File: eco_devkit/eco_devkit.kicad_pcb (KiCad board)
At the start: 2 copper layers, 98.5 x 78 mm, 144 parts, among them J1 USB_C_Receptacle_USB2.0_16P, J10 Micro_SD_Card_Det1, J11 DISPLAY FFC, J2 Conn_02x20_Counter_Clockwise, J3 ADC_SEL1, J4 BluetoothHeader, J5 ADC_SEL1, J6 ADC_SEL1, J7 ADC_SEL1, J8 USB_C_Receptacle_USB2.0_16P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

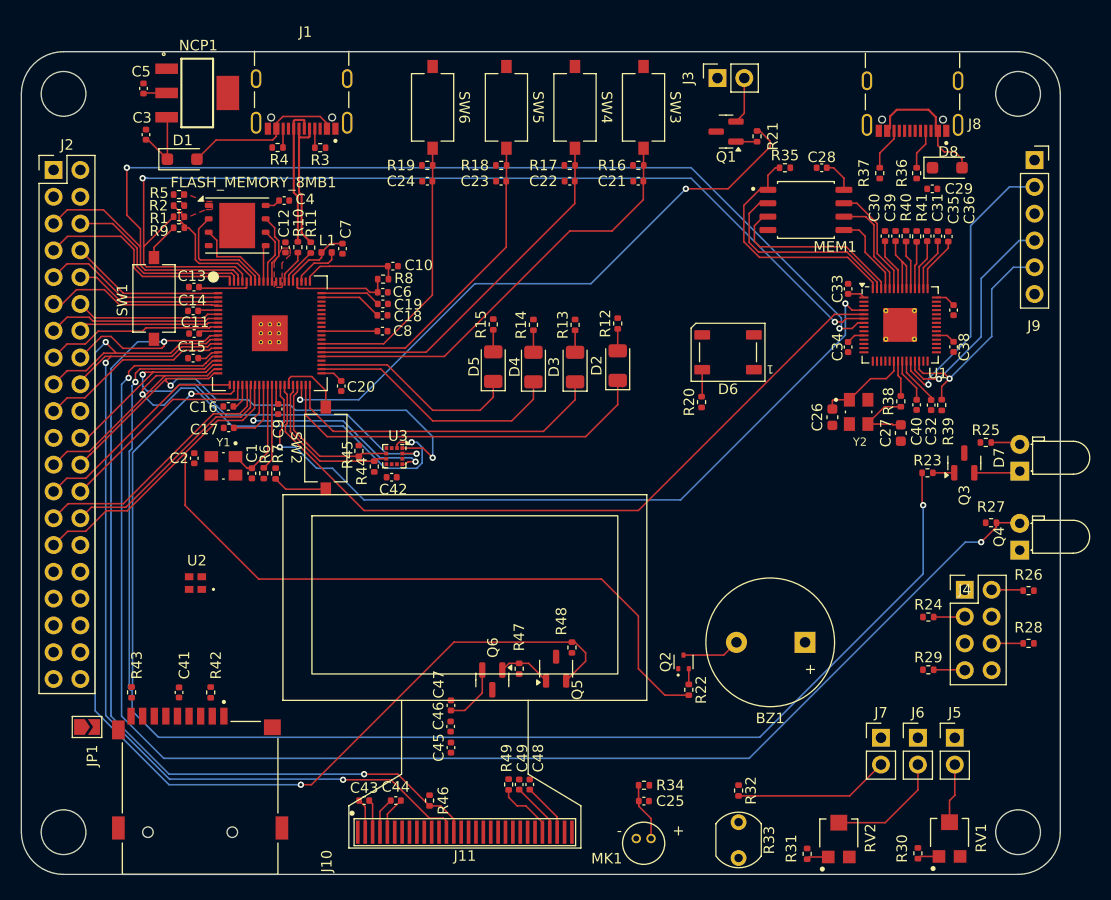
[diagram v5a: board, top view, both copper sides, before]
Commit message: Add all nets
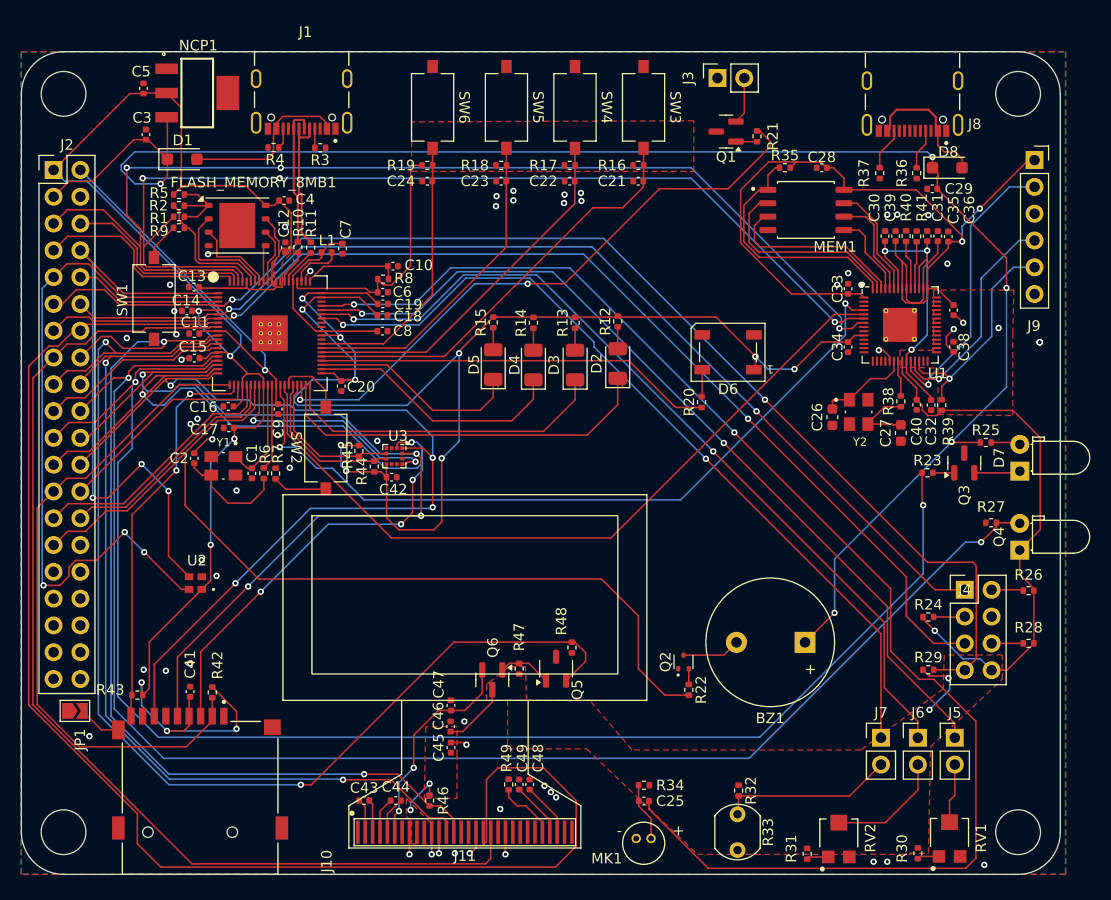
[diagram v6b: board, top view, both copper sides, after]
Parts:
- moved JP1 1.91 mm to (105.1, 112.5)
- moved C41 1.05 mm to (116.0, 110.7), turned to -90 degrees
- moved R33 0.76 mm to (167.9, 122.3)
- moved R43 0.61 mm to (111.0, 111.0), turned to 180 degrees
- moved C14 0.58 mm to (115.7, 74.6)
- moved R4 0.39 mm to (123.9, 59.1)
- moved D3 0.19 mm to (152.5, 79.7)
- moved D4 0.19 mm to (148.6, 79.7)
- moved R13 0.19 mm to (152.5, 75.7)
- moved R14 0.19 mm to (148.6, 75.7)
- moved D2 0.19 mm to (156.5, 79.6)
- moved D5 0.19 mm to (144.7, 79.7)
- moved R12 0.19 mm to (156.5, 75.6)
- moved R15 0.19 mm to (144.7, 75.7)
- moved R42 0.15 mm to (118.1, 110.8)
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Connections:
- C25 pad 2: GPIO44_ADC4 -> GPIO46_ADC6
- C30 pad 1: +1V1 -> +1V1_PROBE
- C31 pad 1: +1V1 -> +1V1_PROBE
- C32 pad 2: +1V1 -> +1V1_PROBE
- J2 pad 40: GPIO43_ADC3 -> GPIO45_ADC5
- J5 pad 1: GPIO43_ADC3 -> GPIO45_ADC5
- J6 pad 1: GPIO45_ADC5 -> GPIO44_ADC4
- J7 pad 1: GPIO46_ADC6 -> GPIO43_ADC3
- RP2350B1 pad 58: GPIO43_ADC3 -> GPIO45_ADC5
- U1 pad 23: +1V1 -> +1V1_PROBE
- U1 pad 45: +1V1 -> +1V1_PROBE
- U1 pad 50: +1V1 -> +1V1_PROBE
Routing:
- net +3V3: track 78.0 -> 481.9 mm, vias 0 -> 24
- net +VBUS: track 6.81 -> 162.4 mm, vias 0 -> 5
- net GPIO46_ADC6: track 0.00 -> 132.2 mm, vias 0 -> 2
- net DISPLAY_SCK: track 14.3 -> 135.6 mm
- net PIN_WIFI_RESET_BL: track 19.8 -> 117.5 mm, vias 0 -> 2
- net PIN_WIFI_TX: track 16.4 -> 107.2 mm, vias 0 -> 2
- net PIN_WIFI_RX: track 13.8 -> 100.7 mm, vias 0 -> 2
- net DISPLAY_MOSI: track 16.9 -> 103.0 mm
- net GPIO45_ADC5: track 0.00 -> 83.7 mm, vias 0 -> 2
- net GPIO44_ADC4: track 0.00 -> 81.2 mm, vias 0 -> 2
- net GPIO43_ADC3: track 0.00 -> 79.3 mm, vias 0 -> 2
- net PIN_LIGHT_SENS_SCL: track 17.4 -> 65.9 mm, vias 0 -> 3
- net PIN_LIGHT_SENS_SDA: track 14.8 -> 57.2 mm, vias 0 -> 3
- net GPIO21: track 20.9 -> 63.2 mm
- net ACCEL_MISO: track 50.2 -> 92.3 mm, vias 2 -> 4
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- added copper zone on B.Cu, net GND
- added copper zone on F.Cu, net GND
- added copper zone on In1.Cu, net GND
- added copper zone on In2.Cu, net GND
- removed copper zone on F.Cu, net (none)
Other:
- copper layers 2 -> 4

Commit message: Finish
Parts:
- added FID1: Fiducial, Fiducial:Fiducial_1mm_Mask2mm, F.Cu at (102.8, 117.0)
- added FID2: Fiducial, Fiducial:Fiducial_1mm_Mask2mm, F.Cu at (174.8, 54.5)
- added FID3: Fiducial, Fiducial:Fiducial_1mm_Mask2mm, F.Cu at (164.2, 96.5)
- added H1: MountingHole, MountingHole:MountingHole_2.7mm_Pad_Via, F.Cu at (194.5, 54.0)
- added H2: MountingHole, MountingHole:MountingHole_2.7mm_Pad_Via, F.Cu at (104.0, 54.0)
- added H3: MountingHole, MountingHole:MountingHole_2.7mm_Pad_Via, F.Cu at (104.0, 124.0)
- added H4: MountingHole, MountingHole:MountingHole_2.7mm_Pad_Via, F.Cu at (194.5, 124.0)
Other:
- outline, holes or cut-outs redrawn
- board text added: "+3V3 SWCLK GND SWDIO RESET NC"
- board text added: "BOOT"
- board text added: "ECODEVKIT P1"
- board text added: "IO36"
- board text added: "IO37"
- board text added: "IO38"
- board text added: "IO39"
- board text added: "RESET"

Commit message: Penultimo
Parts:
- moved FID2 61.4 mm to (115.0, 68.7)
- moved J7 0.39 mm to (181.1, 115.0)
- moved J6 0.25 mm to (184.8, 115.0)
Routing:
- net GPIO45_ADC5: track 83.7 -> 162.4 mm, vias 2 -> 3
- net Net-(J10-GND): track 4.15 -> 60.4 mm, vias 0 -> 6
- net PROBE_GPIO2/SWCLK: track 73.4 -> 105.3 mm, vias 2 -> 3
- net +3V3: track 481.9 -> 498.6 mm, vias 24 -> 26
- net GND: track 22.2 -> 28.7 mm, vias 58 -> 67
- net +1V1: track 56.2 -> 62.5 mm, vias 1 -> 2
- net ACCEL_MOSI: track 96.1 -> 93.1 mm
- net PIN_LED_RED: track 37.7 -> 37.0 mm
- net PROBE_GPIO4/UART_TX: track 97.3 -> 96.8 mm, vias 3 -> 2
- net POBRE_GPIO5/UART_RX: vias 3 -> 2
